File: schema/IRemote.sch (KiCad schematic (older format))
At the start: 18 parts

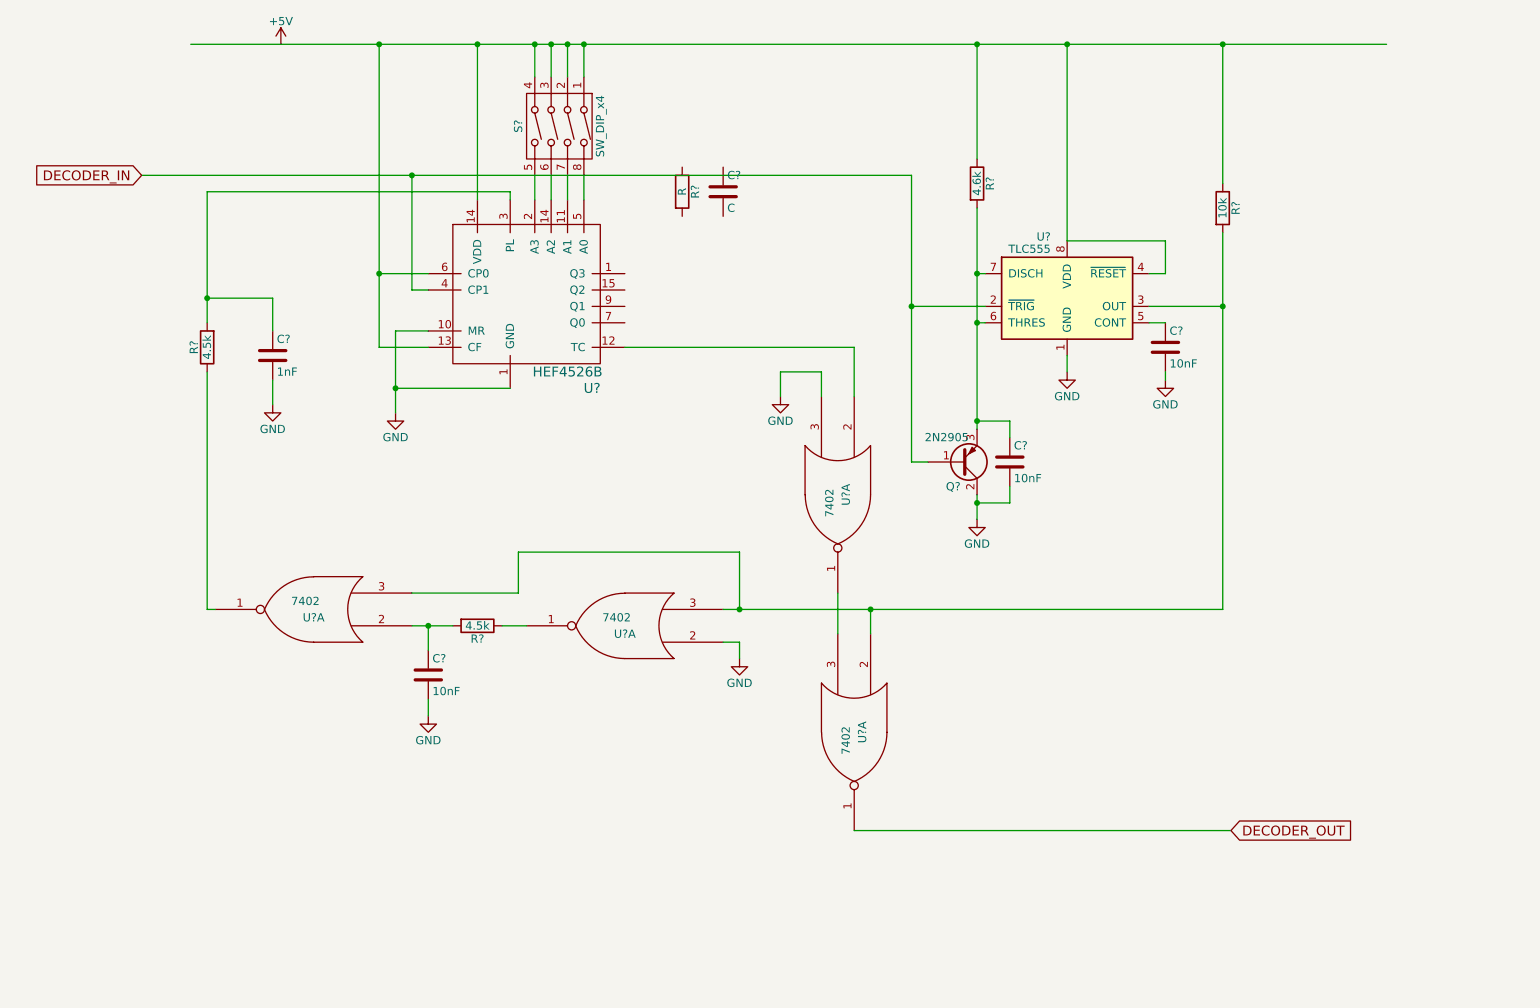
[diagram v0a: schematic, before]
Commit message: add switch pullup
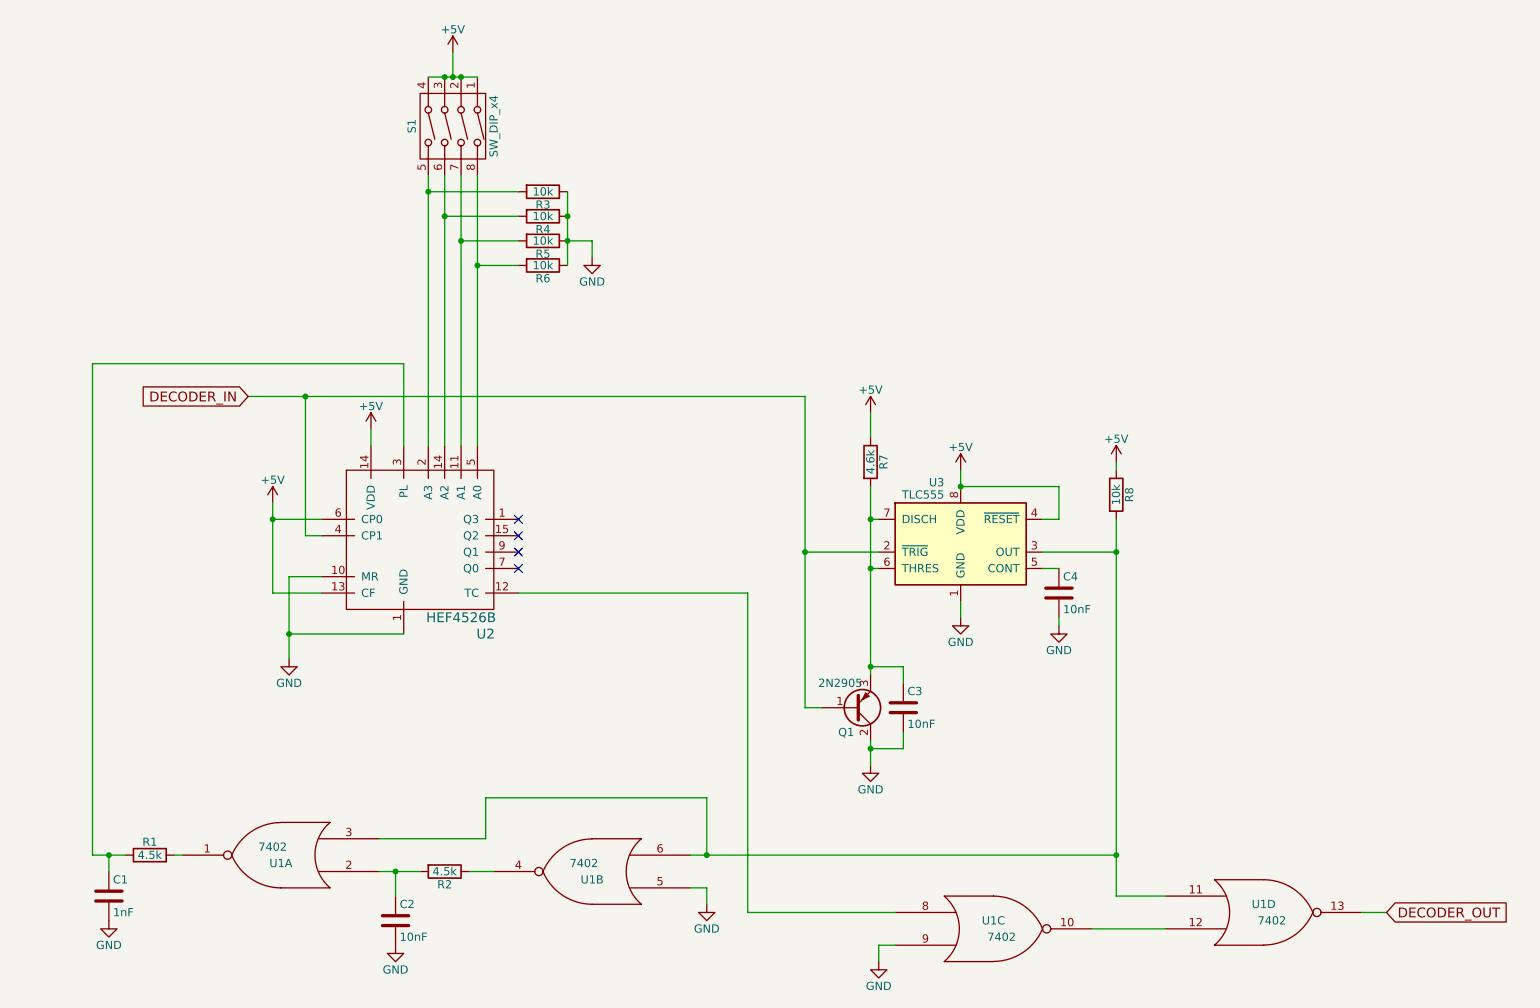
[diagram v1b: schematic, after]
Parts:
- removed C?: C, symbol C
- removed R?: R, symbol R
- added R3, R4, R5, R6: 10k, symbol R
- gave numbers to parts that had none: 13
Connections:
- net +5V: now also R7.1, R8.1, S1.1, S1.2, S1.3, S1.4, U2.13 (CF), U2.14 (VDD), U2.6 (CP0), U3.4 (~RESET), U3.8 (VDD)
- net DECODER_OUT: now also U1.13; no longer U1.1
- net GND: now also U1.5, U1.9, R3.1, R4.1, R5.1, R6.1; no longer U1.2, U1.3
- net at R8.2, U1.3, U3.3 (OUT): now also U1.11, U1.6; no longer U1.2, U1.3
- net at S1.5, U2.2 (A3): now also R3.2
- net at S1.6, U2.14 (VDD): now also R4.2
- net at S1.7, U2.11 (A1): now also R5.2
- net at S1.8, U2.5 (A0): now also R6.2
- net at U2.12 (TC): now also U1.8; no longer U1.2
- net at C1.1, U2.3 (PL): now also R1.1; no longer R1.2
- net at U1.1: now also R1.2; no longer R1.1
- net at R2.1: now also U1.4; no longer U1.1
- new net: U1.10, U1.12
- no-connect marks 0 -> 4
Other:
- moved on the sheet: C1, C2, C3, C4, Q1, R1, R2, R7, R8, S1, U1A, U2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

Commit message: Use hierarchical schematic
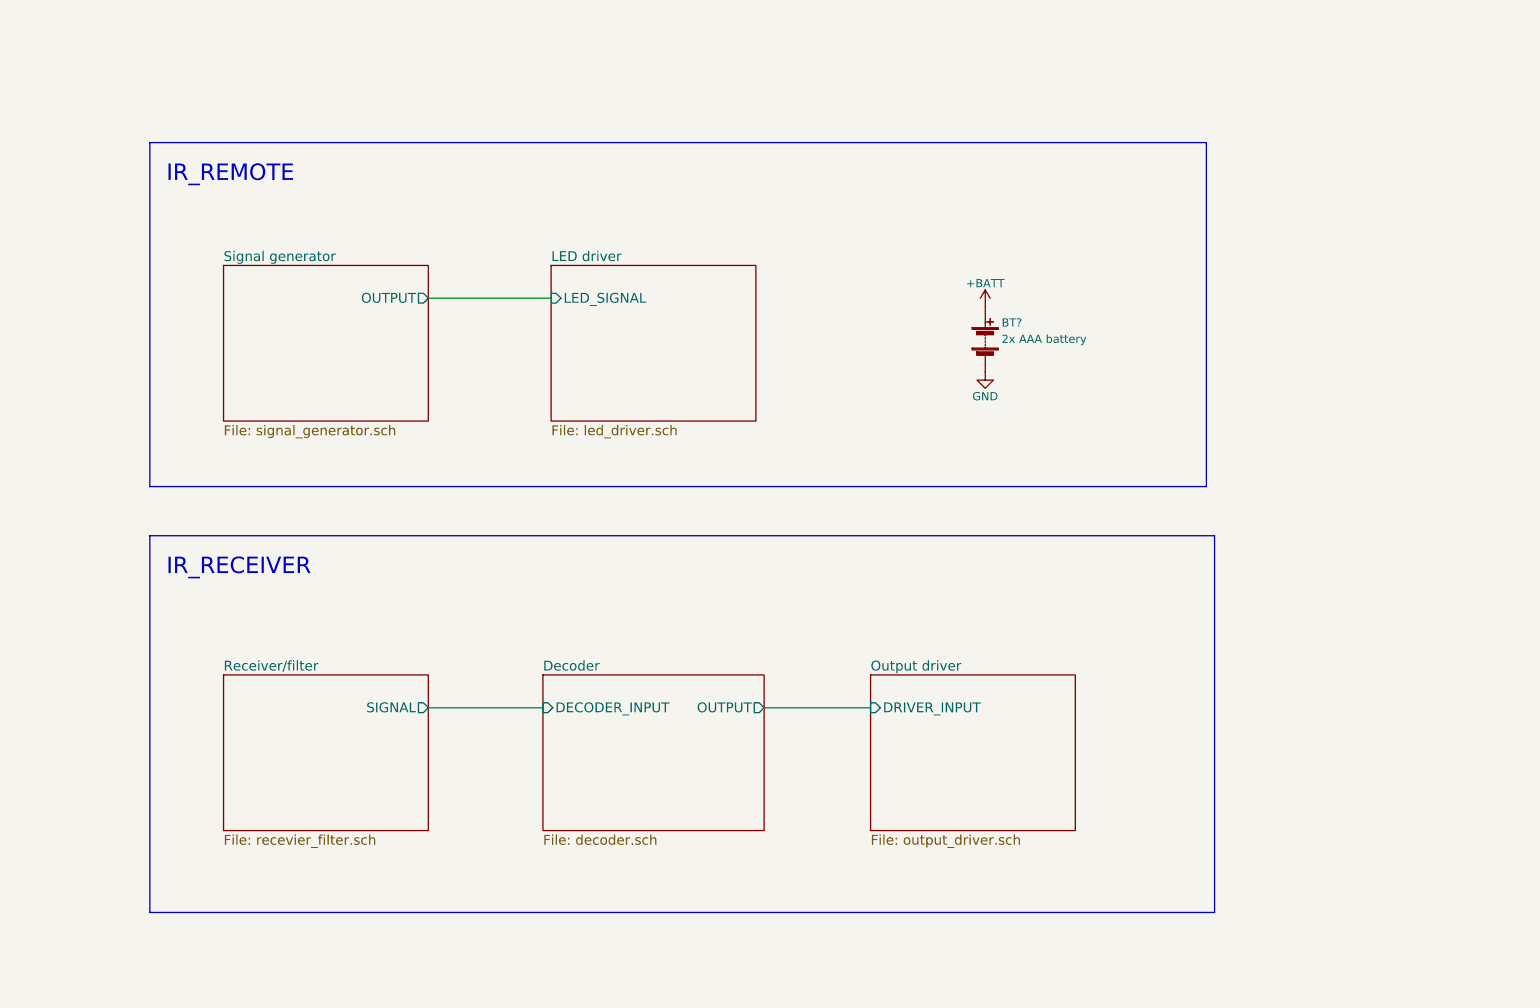
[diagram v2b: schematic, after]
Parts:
- removed C1: 1nF, symbol C
- removed C2, C3, C4: 10nF, symbol C
- removed Q1: 2N2905, symbol Q_PNP_BCE
- removed R1, R2: 4.5k, symbol R
- removed R3, R4, R5, R6, R8: 10k, symbol R
- removed R7: 4.6k, symbol R
- removed S1: SW_DIP_x4, symbol SW_DIP_x4
- removed U1: 7402, symbol 7402
- removed U2: HEF4526B, symbol HEF4526B
- removed U3: TLC555, symbol TLC555
- added BT?: 2x AAA battery, symbol Battery
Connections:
- net GND: now also BT?.2 (-)
- new net +BATT: BT?.1 (+)
- no-connect marks 4 -> 0
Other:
- note added: "IR_RECEIVER"
- note added: "IR_REMOTE"
